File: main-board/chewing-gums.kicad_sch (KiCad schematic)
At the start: 18 parts, among them J10 Conn_02x16_Odd_Even, J3 Conn_02x16_Odd_Even, J6 Conn_02x16_Odd_Even, J7 Conn_02x16_Odd_Even, J9 Conn_02x16_Odd_Even

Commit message: Before re-organizing the main board
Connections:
- net Vout_5_A is gone; now on net VDD_IO: CG5.1 (OUT_1), CG5.2 (OUT_2), CG5.21 (OUT_0)
- net 3V3: now also J10.13 (Pin_13), J10.14 (Pin_14)
- net 5V: now also CG1.12 (5V), CG1.13 (5V), CG10.12 (5V), CG10.13 (5V), CG11.12 (5V), CG11.13 (5V), CG12.12 (5V), CG12.13 (5V), CG2.12 (5V), CG2.13 (5V), CG3.12 (5V), CG3.13 (5V), CG4.12 (5V), CG4.13 (5V), CG5.12 (5V), CG5.13 (5V), CG6.12 (5V), CG6.13 (5V), CG7.12 (5V), CG7.13 (5V), CG8.12 (5V), CG8.13 (5V), CG9.12 (5V), CG9.13 (5V), J10.17 (Pin_17), J10.18 (Pin_18)
- net A3V3: now also J10.5 (Pin_5), J10.6 (Pin_6)
- net GND: now also J10.11 (Pin_11), J10.12 (Pin_12), J10.15 (Pin_15), J10.16 (Pin_16), J10.19 (Pin_19), J10.20 (Pin_20), J10.3 (Pin_3), J10.4 (Pin_4), J10.7 (Pin_7), J10.8 (Pin_8), J3.1 (Pin_1), J3.17 (Pin_17), J3.18 (Pin_18), J3.2 (Pin_2), J3.27 (Pin_27), J3.28 (Pin_28), J3.7 (Pin_7), J3.8 (Pin_8), J6.13 (Pin_13), J6.14 (Pin_14), J6.23 (Pin_23), J6.24 (Pin_24), J6.5 (Pin_5), J6.6 (Pin_6), J7.13 (Pin_13), J7.14 (Pin_14), J7.19 (Pin_19), J7.20 (Pin_20), J7.23 (Pin_23), J7.24 (Pin_24), J7.29 (Pin_29), J7.30 (Pin_30), J7.32 (Pin_32), J7.5 (Pin_5), J7.6 (Pin_6), J9.1 (Pin_1), J9.11 (Pin_11), J9.12 (Pin_12), J9.2 (Pin_2), J9.21 (Pin_21), J9.22 (Pin_22), J9.31 (Pin_31), J9.32 (Pin_32)
- net REF: now also J10.1 (Pin_1), J10.2 (Pin_2)
- net SCL: now also CG1.6 (SCL), CG10.6 (SCL), CG11.6 (SCL), CG12.6 (SCL), CG2.6 (SCL), CG3.6 (SCL), CG4.6 (SCL), CG5.6 (SCL), CG6.6 (SCL), CG7.6 (SCL), CG8.6 (SCL), CG9.6 (SCL), J10.10 (Pin_10); no longer CG1.13 (SCL), CG10.13 (SCL), CG11.13 (SCL), CG12.13 (SCL), CG2.13 (SCL), CG3.13 (SCL), CG4.13 (SCL), CG5.13 (SCL), CG6.13 (SCL), CG7.13 (SCL), CG8.13 (SCL), CG9.13 (SCL)
- net SDA: now also CG1.7 (SDA), CG10.7 (SDA), CG11.7 (SDA), CG12.7 (SDA), CG2.7 (SDA), CG3.7 (SDA), CG4.7 (SDA), CG5.7 (SDA), CG6.7 (SDA), CG7.7 (SDA), CG8.7 (SDA), CG9.7 (SDA), J10.9 (Pin_9); no longer CG1.12 (SDA), CG10.12 (SDA), CG11.12 (SDA), CG12.12 (SDA), CG2.12 (SDA), CG3.12 (SDA), CG4.12 (SDA), CG5.12 (SDA), CG6.12 (SDA), CG7.12 (SDA), CG8.12 (SDA), CG9.12 (SDA)
- net Vout_10_A: now also J9.15 (Pin_15), J9.16 (Pin_16)
- net Vout_10_B: now also J9.14 (Pin_14)
- net Vout_10_diff: now also J9.13 (Pin_13)
- net Vout_11_A: now also J9.10 (Pin_10), J9.9 (Pin_9)
- net Vout_11_B: now also J9.8 (Pin_8)
- net Vout_11_diff: now also J9.7 (Pin_7)
- net Vout_12_A: now also J9.5 (Pin_5), J9.6 (Pin_6)
- net Vout_12_B: now also J9.4 (Pin_4)
- net Vout_3_A: now also J3.5 (Pin_5), J3.6 (Pin_6)
- net Vout_3_B: now also J3.4 (Pin_4)
- net Vout_3_diff: now also J3.3 (Pin_3)
- net Vout_4_A: now also J6.3 (Pin_3), J6.4 (Pin_4)
- net Vout_4_B: now also J6.2 (Pin_2)
- net Vout_4_diff: now also J6.1 (Pin_1)
- net Vout_5_B: now also J7.26 (Pin_26)
- net Vout_5_diff: now also J7.25 (Pin_25)
- net Vout_6_A: now also J7.3 (Pin_3), J7.4 (Pin_4)
- net Vout_6_B: now also J7.2 (Pin_2)
- net Vout_6_diff: now also J7.1 (Pin_1)
- net Vout_7_A: now also J9.29 (Pin_29), J9.30 (Pin_30)
- net Vout_7_B: now also J9.28 (Pin_28)
- net Vout_7_diff: now also J9.27 (Pin_27)
- net Vout_8_A: now also J9.25 (Pin_25), J9.26 (Pin_26)
- net Vout_8_B: now also J9.24 (Pin_24)
- net Vout_8_diff: now also J9.23 (Pin_23); no longer CG12.20 (OUT_4)
- net Vout_9_A: now also J9.19 (Pin_19), J9.20 (Pin_20)
- net Vout_9_B: now also J9.18 (Pin_18)
- net Vout_9_diff: now also J9.17 (Pin_17)
- net GPIO_11: now reaches J3.10 (Pin_10)
- net GPIO_12: now reaches J3.11 (Pin_11)
- net GPIO_13: now reaches J3.12 (Pin_12)
- net GPIO_14: now reaches J3.13 (Pin_13)
- net GPIO_15: now reaches J3.14 (Pin_14)
- net GPIO_16: now reaches J3.15 (Pin_15)
- net GPIO_17: now reaches J3.16 (Pin_16)
- net GPIO_18: now reaches J3.19 (Pin_19)
- net GPIO_19: now reaches J3.20 (Pin_20)
- net GPIO_20: now reaches J3.21 (Pin_21)
- net GPIO_21: now reaches J3.22 (Pin_22)
- net GPIO_22: now reaches J3.23 (Pin_23)
- net GPIO_22: now also J3.24 (Pin_24)
- net GPIO_24: now reaches J3.25 (Pin_25)
- net GPIO_25: now reaches J3.26 (Pin_26)
- net GPIO_10: now reaches J3.9 (Pin_9)
- net EXIT_VALUE: now reaches J6.10 (Pin_10)
- net BOOT_SEL: now reaches J6.11 (Pin_11)
- net GPIO_2: now reaches J6.15 (Pin_15)
- net GPIO_3: now reaches J6.16 (Pin_16)
- net GPIO_4: now reaches J6.17 (Pin_17)
- net GPIO_5: now reaches J6.18 (Pin_18)
- net GPIO_6: now reaches J6.19 (Pin_19)
- net GPIO_7: now reaches J6.20 (Pin_20)
- net GPIO_8: now reaches J6.21 (Pin_21)
- net GPIO_9: now reaches J6.22 (Pin_22)
- net SPI_FLASH_CS0: now reaches J6.25 (Pin_25)
- net SPI_FLASH_CS1: now reaches J6.26 (Pin_26)
- net SPI_FLASH_SD2: now reaches J6.27 (Pin_27)
- net SPI_FLASH_SD3: now reaches J6.28 (Pin_28)
- net SPI_FLASH_SD0: now reaches J6.29 (Pin_29)
- net SPI_FLASH_SD1: now reaches J6.30 (Pin_30)
- net SPI_FLASH_SCK: now reaches J6.31 (Pin_31)
- net nRST: now reaches J6.7 (Pin_7)
- net EXEC_FLASH: now reaches J6.8 (Pin_8)
- net EXIT_VALID: now reaches J6.9 (Pin_9)
- net Vout_12_diff: now reaches J9.3 (Pin_3)
- net Vout_12_diff: now also CG12.20 (OUT_4)
- net SPI_S_SCK: now reaches J7.10 (Pin_10)
- net SPI_S_MOSI: now reaches J7.11 (Pin_11)
- net SPI_S_MISO: now reaches J7.12 (Pin_12)
- net JTAG_TCK: now reaches J7.15 (Pin_15)
- net JTAG_TMS: now reaches J7.16 (Pin_16)
- net JTAG_TD0: now reaches J7.17 (Pin_17)
- net JTAG_TDI: now reaches J7.18 (Pin_18)
- net UART_TX: now reaches J7.21 (Pin_21)
- net UART_RX: now reaches J7.22 (Pin_22)
- net VDD_IO: now reaches J7.27 (Pin_27)
- net VDD_IO: now also J7.28 (Pin_28)
- net clk: now reaches J7.31 (Pin_31)
- net GPIO_0: now reaches J7.7 (Pin_7)
- net GPIO_1: now reaches J7.8 (Pin_8)
- net SPI_S_CS: now reaches J7.9 (Pin_9)
- no-connect marks 59 -> 35
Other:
- moved on the sheet: CG1, CG10, CG11, CG12, CG2, CG3, CG4, CG5, CG6, CG7, CG8, CG9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

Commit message: Before re-routing programmer
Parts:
- removed J10, J3, J6, J7, J9: Conn_02x16_Odd_Even, symbol Connector_Generic:Conn_02x16_Odd_Even
- added U5: ~, heep_footprints:adc-dac, symbol cheeps-tb:adc-dac
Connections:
- net 3V3: now also U5.3 (3V3), U5.4 (3V3)
- net 5V: now also U5.1 (5V), U5.2 (5V)
- net DAC_4: now also U5.29 (IO17); no longer U4.29 (IO17)
- net DAC_5: now also U5.30 (IO18); no longer U4.30 (IO18)
- net DAC_6: now also U5.31 (IO19); no longer U4.31 (IO19)
- net DAC_7: now also U5.32 (IO20); no longer U4.32 (IO20)
- net GND: now also U5.13 (GND), U5.20 (GND), U5.21 (GND), U5.35 (GND), U5.36 (A3V3), U5.7 (GND), U5.8 (GND)
- net SCL: now also U5.6 (SCL)
- net SDA: now also U5.5 (SDA)
- net A3V3 renamed A3V3_A
- net A3V3_A: no longer CG10.15 (3V3), CG11.15 (3V3), CG12.15 (3V3), CG7.15 (3V3), CG8.15 (3V3), CG9.15 (3V3)
- net EN_1 renamed EN_CG_1
- net EN_10 renamed EN_CG_10
- net EN_11 renamed EN_CG_11
- net EN_12 renamed EN_CG_12
- net EN_2 renamed EN_CG_2
- net EN_3 renamed EN_CG_3
- net EN_4 renamed EN_CG_4
- net EN_5 renamed EN_CG_5
- net EN_6 renamed EN_CG_6
- net EN_7 renamed EN_CG_7
- net EN_8 renamed EN_CG_8
- net EN_9 renamed EN_CG_9
- net REF renamed REF_A
- net REF_A: no longer CG10.16 (REF), CG11.16 (REF), CG12.16 (REF), CG7.16 (REF), CG8.16 (REF), CG9.16 (REF)
- net VDD_IO renamed Vout_A_5
- net Vout_10_A renamed Vout_A_10
- net Vout_10_B renamed Vout_B_10
- net Vout_10_diff: no longer names the net of U4.23 (IO11)
- net Vout_10_diff: no longer CG10.20 (OUT_4)
- net Vout_11_A renamed Vout_A_11
- net Vout_11_B renamed Vout_B_11
- net Vout_11_diff renamed Vout_diff_11
- net Vout_12_A renamed Vout_A_12
- net Vout_12_B renamed Vout_B_12
- net Vout_12_diff renamed Vout_diff_12
- net Vout_1_A renamed Vout_A_1
- net Vout_1_B renamed Vout_B_1
- net Vout_1_diff renamed Vout_diff_1
- net Vout_2_A renamed Vout_A_2
- net Vout_2_B renamed Vout_B_2
- net Vout_2_diff renamed Vout_diff_2
- net Vout_3_A renamed Vout_A_3
- net Vout_3_B renamed Vout_B_3
- net Vout_3_diff renamed Vout_diff_3
- net Vout_4_A renamed Vout_A_4
- net Vout_4_B renamed Vout_B_4
- net Vout_4_diff renamed Vout_diff_4
- net Vout_5_B renamed Vout_B_5
- net Vout_5_diff renamed Vout_diff_5
- net Vout_6_A renamed Vout_A_6
- net Vout_6_B renamed Vout_B_6
- net Vout_6_diff renamed Vout_diff_6
- net Vout_7_A renamed Vout_A_7
- net Vout_7_B renamed Vout_B_7
- net Vout_7_diff: no longer names the net of U4.26 (IO14)
- net Vout_7_diff: no longer CG7.20 (OUT_4)
- net Vout_8_A renamed Vout_A_8
- net Vout_8_B renamed Vout_B_8
- net Vout_8_diff: no longer names the net of U4.25 (IO13)
- net Vout_8_diff: no longer CG8.20 (OUT_4)
- net Vout_9_A renamed Vout_A_9
- net Vout_9_B renamed Vout_B_9
- net Vout_9_diff: no longer names the net of U4.24 (IO12)
- net Vout_9_diff: no longer CG9.20 (OUT_4)
- new net A3V3_B: CG10.15 (3V3), CG11.15 (3V3), CG12.15 (3V3), CG7.15 (3V3), CG8.15 (3V3), CG9.15 (3V3), U5.37 (A3V3), U5.38 (GND)
- new net REF_B: CG10.16 (REF), CG11.16 (REF), CG12.16 (REF), CG7.16 (REF), CG8.16 (REF), CG9.16 (REF), U5.39 (REF), U5.40 (REF)
- new net Vout_diff_10: CG10.20 (OUT_4), U5.23 (IO11)
- new net Vout_diff_7: CG7.20 (OUT_4), U5.26 (IO14)
- new net Vout_diff_8: CG8.20 (OUT_4), U5.25 (IO13)
- new net Vout_diff_9: CG9.20 (OUT_4), U5.24 (IO12)
- no-connect marks 35 -> 42
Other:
- note added: "VDD IO cheep"
- note added: "VDD IO main"
- moved on the sheet: CG1, CG10, CG11, CG12, CG2, CG3, CG4, CG5, CG6, CG7, CG8, CG9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

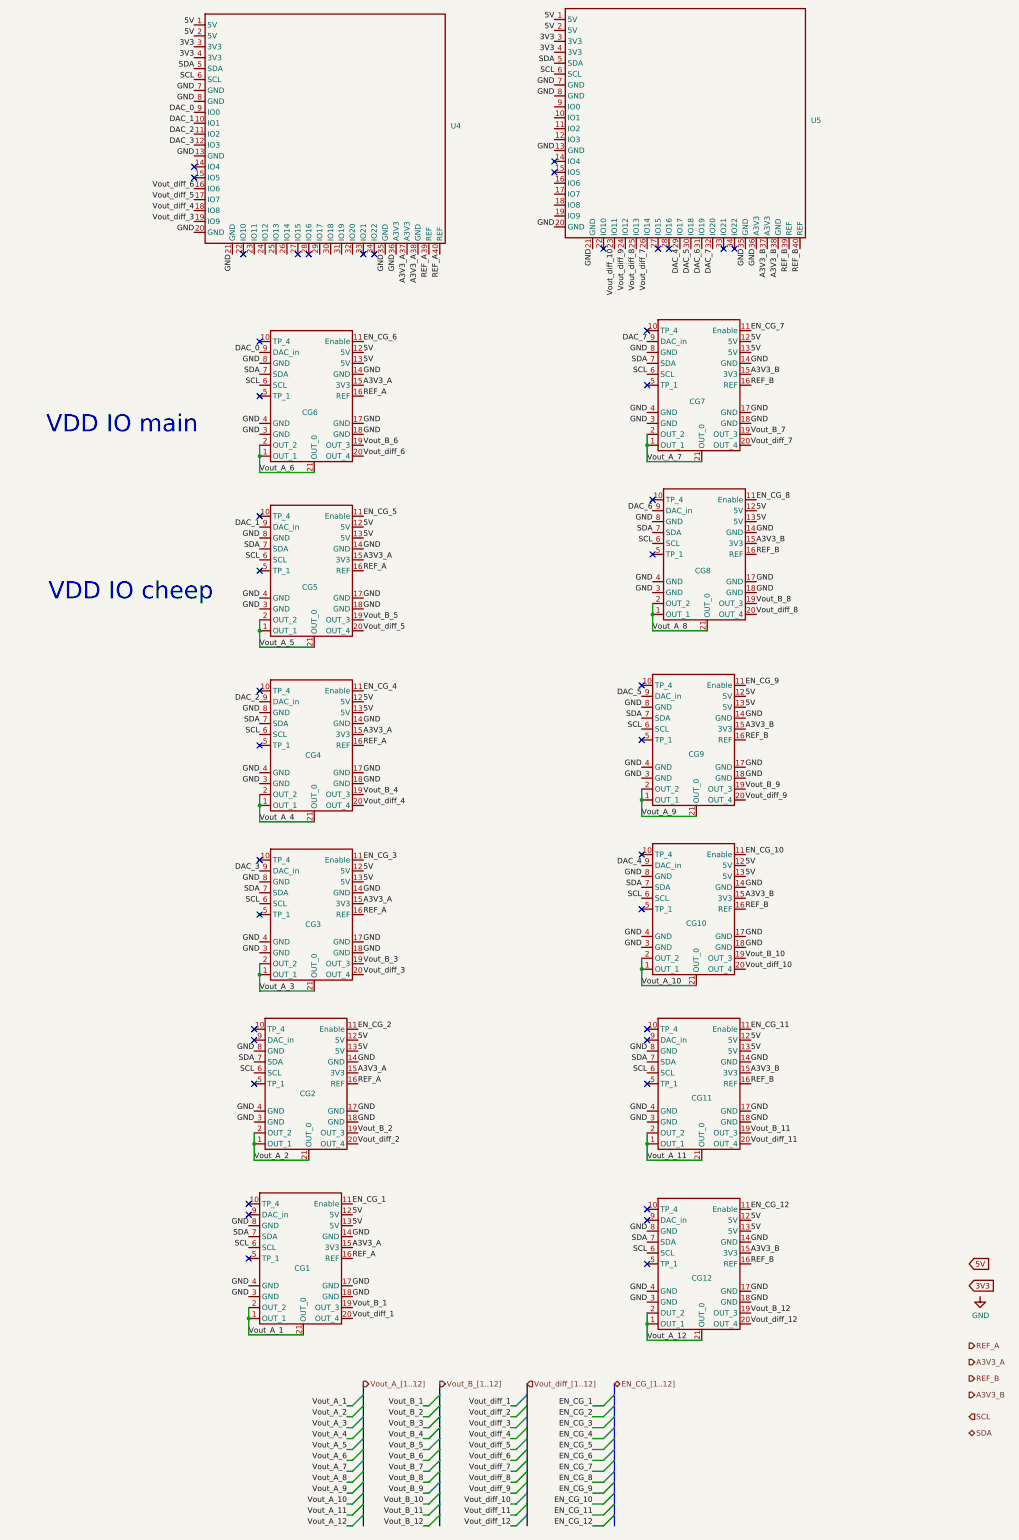
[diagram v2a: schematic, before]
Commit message: WIP: added i2c expanders and re-structuring i2c distributino
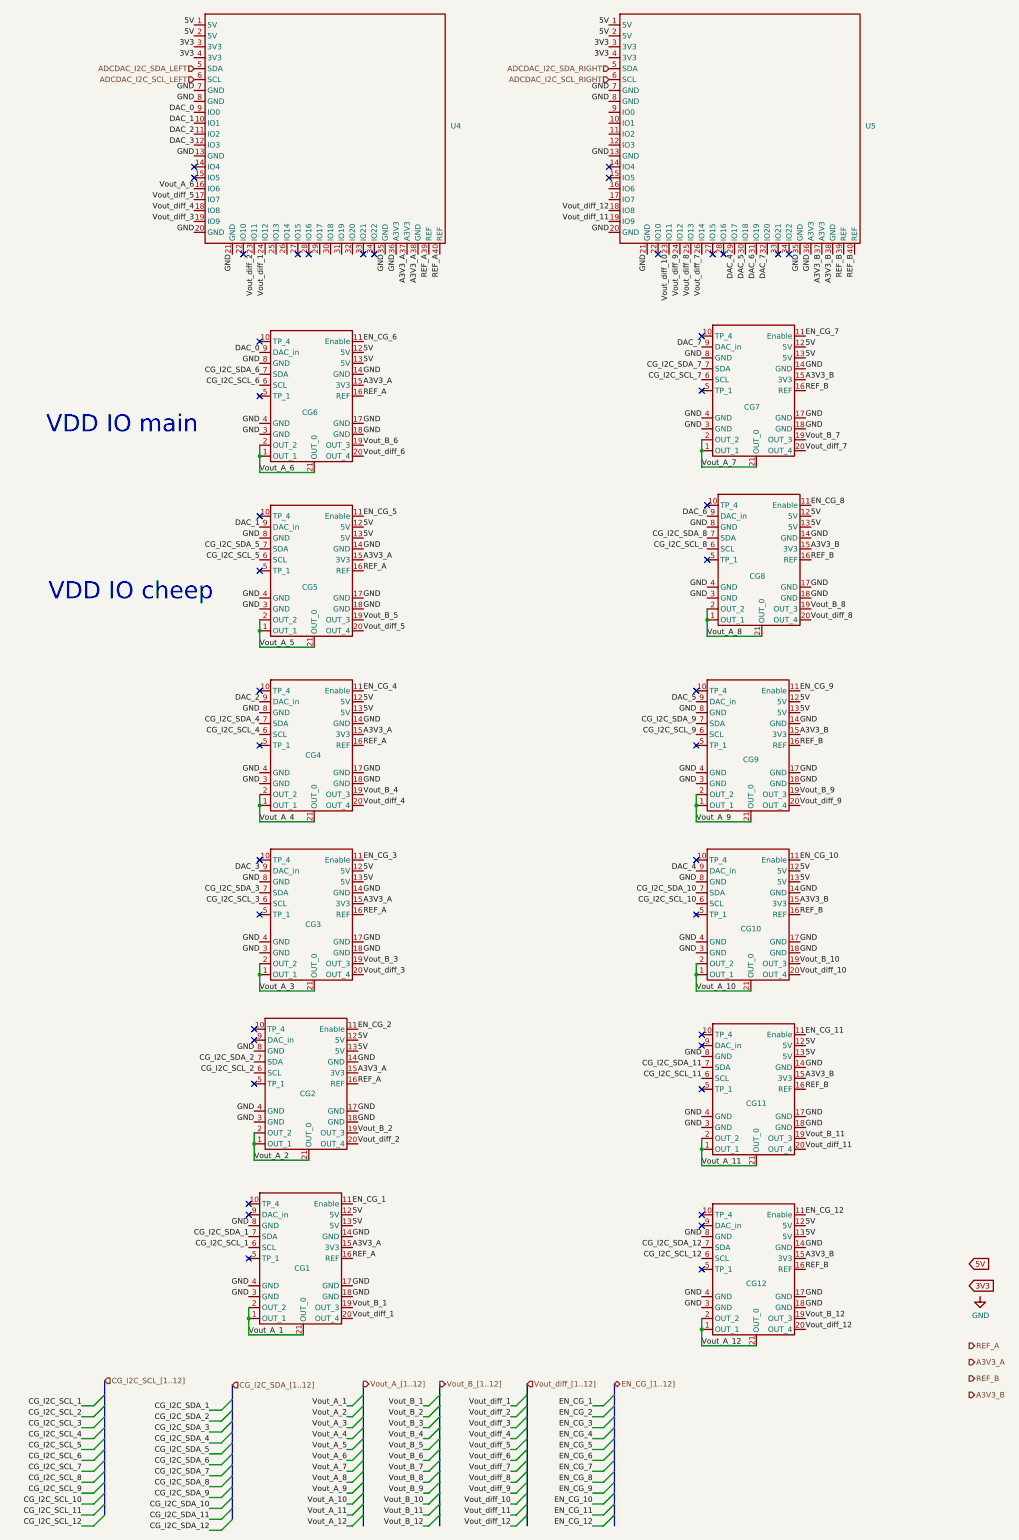
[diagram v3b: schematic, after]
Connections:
- net Vout_A_6: now also U4.16 (IO6)
- net Vout_diff_1: now also U4.24 (IO12)
- net Vout_diff_11: now also U5.19 (IO9)
- net Vout_diff_12: now also U5.18 (IO8)
- net Vout_diff_2: now also U4.23 (IO11)
- net Vout_diff_6: no longer U4.16 (IO6)
- removed net SCL: CG1.6 (SCL), CG10.6 (SCL), CG11.6 (SCL), CG12.6 (SCL), CG2.6 (SCL), CG3.6 (SCL), CG4.6 (SCL), CG5.6 (SCL), CG6.6 (SCL), CG7.6 (SCL), CG8.6 (SCL), CG9.6 (SCL), U4.6 (SCL), U5.6 (SCL)
- removed net SDA: CG1.7 (SDA), CG10.7 (SDA), CG11.7 (SDA), CG12.7 (SDA), CG2.7 (SDA), CG3.7 (SDA), CG4.7 (SDA), CG5.7 (SDA), CG6.7 (SDA), CG7.7 (SDA), CG8.7 (SDA), CG9.7 (SDA), U4.5 (SDA), U5.5 (SDA)
- new net ADCDAC_I2C_SCL_LEFT: U4.6 (SCL)
- new net ADCDAC_I2C_SCL_RIGHT: U5.6 (SCL)
- new net ADCDAC_I2C_SDA_LEFT: U4.5 (SDA)
- new net ADCDAC_I2C_SDA_RIGHT: U5.5 (SDA)
- new net CG_I2C_SCL_1: CG1.6 (SCL)
- new net CG_I2C_SCL_10: CG10.6 (SCL)
- new net CG_I2C_SCL_11: CG11.6 (SCL)
- new net CG_I2C_SCL_12: CG12.6 (SCL)
- new net CG_I2C_SCL_2: CG2.6 (SCL)
- new net CG_I2C_SCL_3: CG3.6 (SCL)
- new net CG_I2C_SCL_4: CG4.6 (SCL)
- new net CG_I2C_SCL_5: CG5.6 (SCL)
- new net CG_I2C_SCL_6: CG6.6 (SCL)
- new net CG_I2C_SCL_7: CG7.6 (SCL)
- new net CG_I2C_SCL_8: CG8.6 (SCL)
- new net CG_I2C_SCL_9: CG9.6 (SCL)
- new net CG_I2C_SDA_1: CG1.7 (SDA)
- new net CG_I2C_SDA_10: CG10.7 (SDA)
- new net CG_I2C_SDA_11: CG11.7 (SDA)
- new net CG_I2C_SDA_12: CG12.7 (SDA)
- new net CG_I2C_SDA_2: CG2.7 (SDA)
- new net CG_I2C_SDA_3: CG3.7 (SDA)
- new net CG_I2C_SDA_4: CG4.7 (SDA)
- new net CG_I2C_SDA_5: CG5.7 (SDA)
- new net CG_I2C_SDA_6: CG6.7 (SDA)
- new net CG_I2C_SDA_7: CG7.7 (SDA)
- new net CG_I2C_SDA_8: CG8.7 (SDA)
- new net CG_I2C_SDA_9: CG9.7 (SDA)
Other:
- moved on the sheet: CG10, CG11, CG12, CG7, CG8, CG9, U5
